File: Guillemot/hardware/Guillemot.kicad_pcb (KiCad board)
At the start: 4 copper layers, 55.5 x 44 mm, 33 parts, among them Q1 IPB042N10N3G, Q2 AO3422, Q3 SI2309CDS, Q4 2N7002, Q5 MMBT3904, Q6 MMBT3904, U1 XIAO-nRF52840-SMD, U2 SN74LVC2G02DCTR

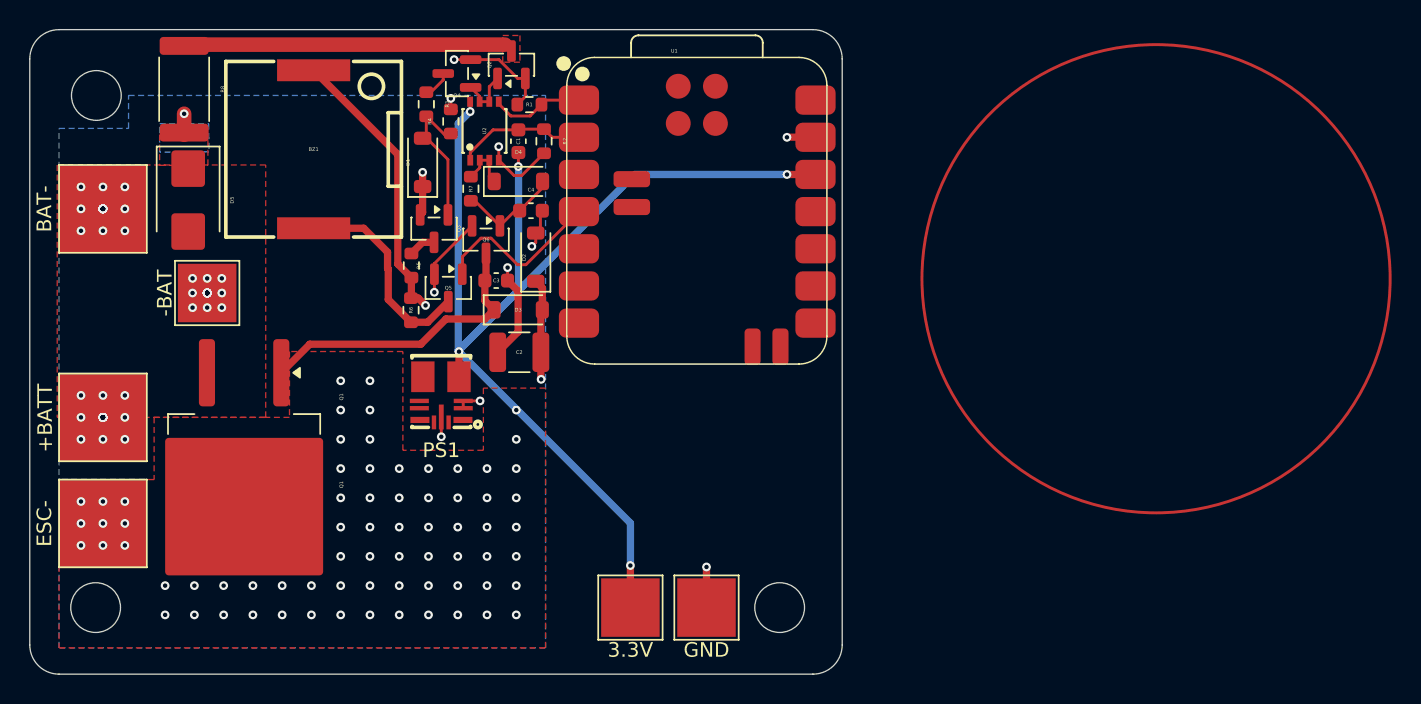
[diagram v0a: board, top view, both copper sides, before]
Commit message: Update C2 to EMK325ABJ107MM-P, add no-hardware-edits rule, add codebase docs
- C2: EMK325ABJ107MM-P 100µF 16V X5R (was CL32A107MPVNNNE 10V)
- Cursor rule: do not modify files under hardware/
- Guillemot: KiCad schematic/PCB LCSC C90143, README, matched parts
- logs/18-CODEBASE_TECHNICAL_DOCUMENTATION.md

Made-with: Cursor
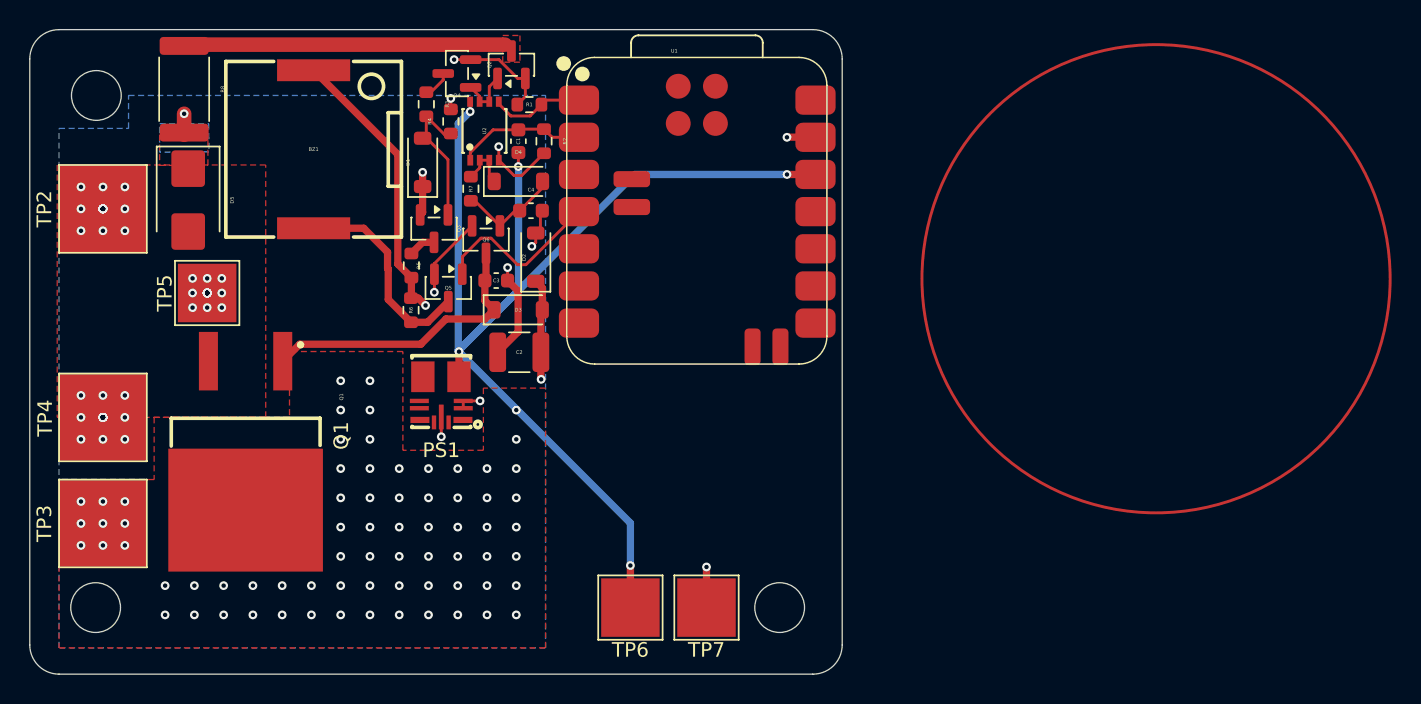
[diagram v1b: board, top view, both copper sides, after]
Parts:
- Q1: footprint Package_TO_SOT_SMD:TO-263-2 -> easyeda2kicad:TO-263-2_L10.0-W9.1-P5.08-LS15.2-TL
- moved Q1 3.35 mm to (102.5, 62.8)
- renumbered BAT- to TP2, ESC- to TP3, +BATT to TP4, -BAT to TP5, 3.3V to TP6, GND to TP7
